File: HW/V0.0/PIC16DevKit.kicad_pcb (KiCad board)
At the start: 4 copper layers, 68.8 x 54 mm, 100 parts, among them J1 9V-12V, J2 USB C, J3 EXP PORT, J4 SIL04, J5 QWIIC, Q1 SI2301, Q3 SI2301, Q4 2N3906, Q5 SI2302, Q6 SI2302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

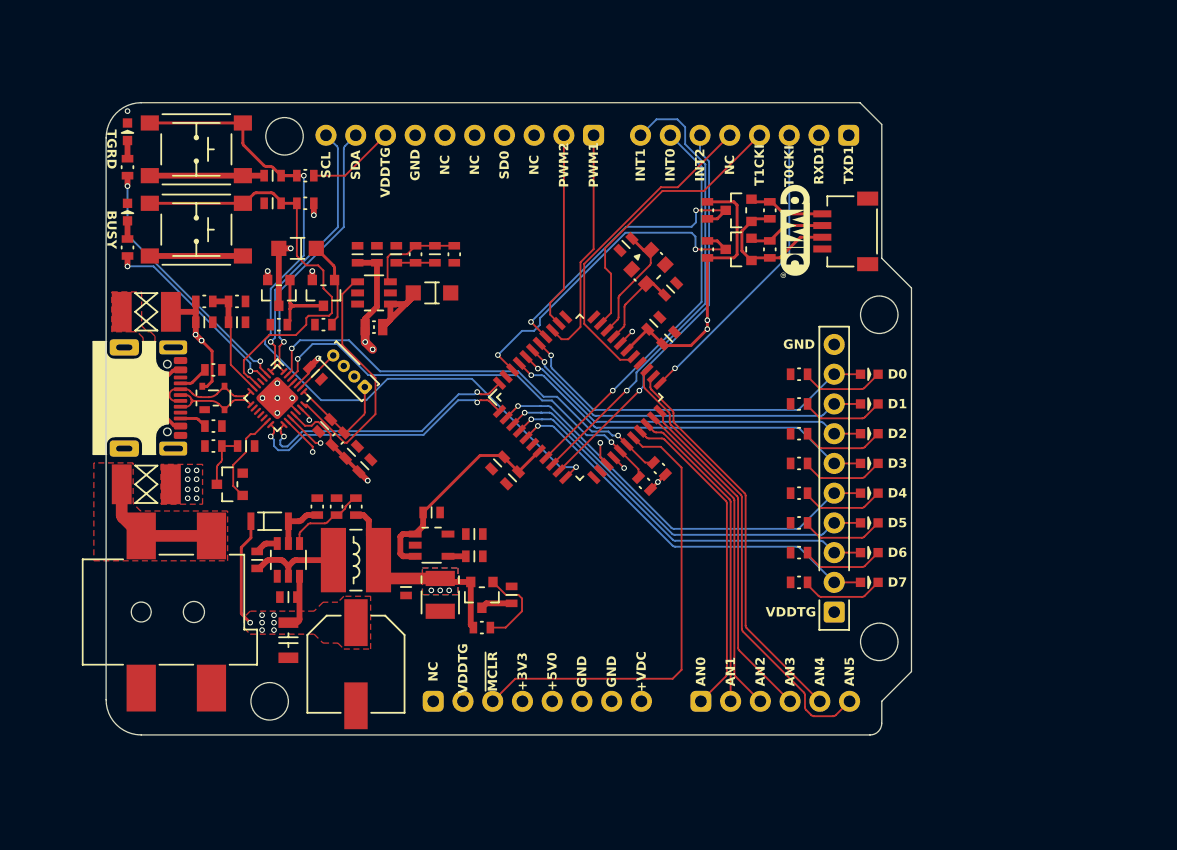
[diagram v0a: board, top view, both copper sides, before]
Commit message: PIC16-DevKit-PCB-877 layout update 2-miss via gnd
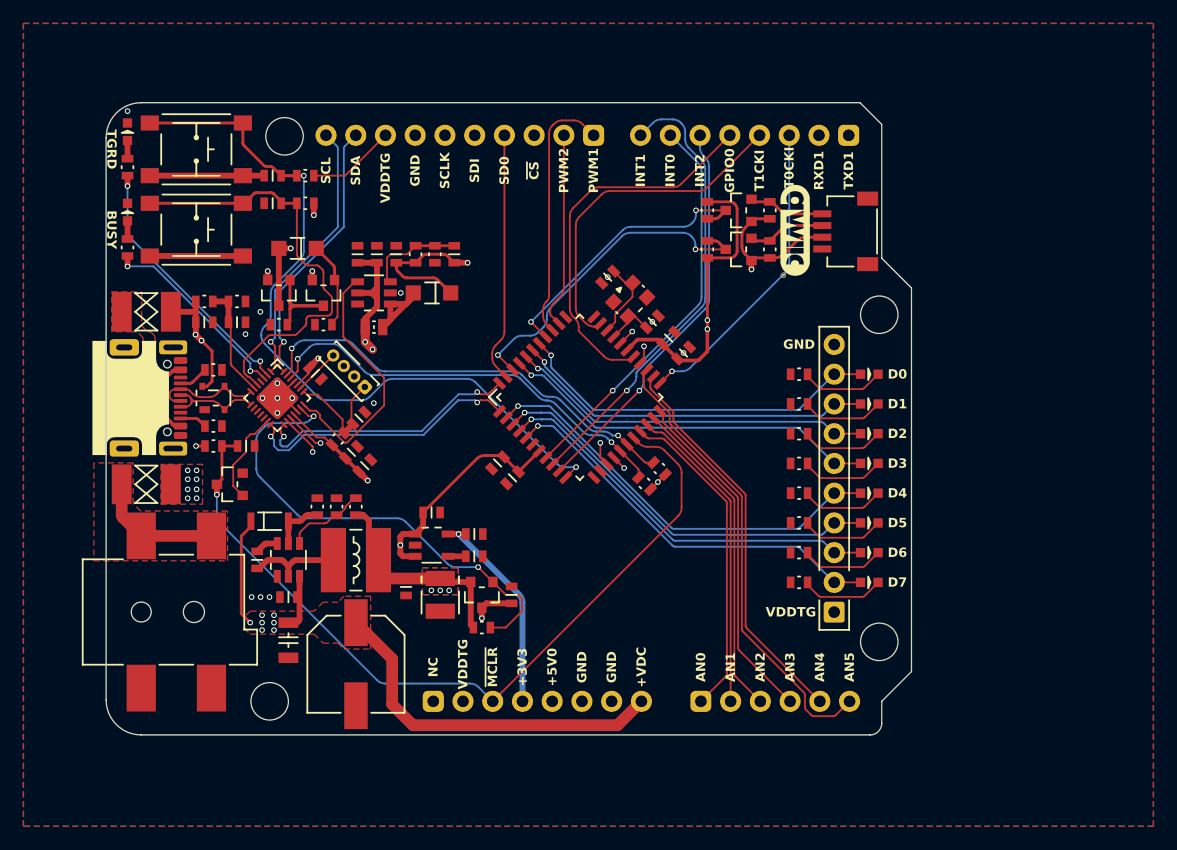
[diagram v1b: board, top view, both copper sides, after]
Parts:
- moved C15 3.20 mm to (107.3, 61.7)
- moved U10 3.20 mm to (105.4, 59.8)
- moved C16 3.20 mm to (103.5, 57.9)
- moved C32 2.99 mm to (82.3, 70.0), turned to -135 degrees
- moved C20 1.80 mm to (108.7, 63.1)
- moved C21 1.80 mm to (110.0, 64.4)
- moved C12 1.65 mm to (90.4, 56.0)
- moved R10 1.65 mm to (88.8, 56.0)
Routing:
- net +3.3V: track 12.5 -> 72.0 mm, vias 0 -> 2
- net VPP: track 3.30 -> 57.8 mm, vias 0 -> 2
- net /TARGET MCU/SCLK: track 1.26 -> 36.5 mm
- net /POWER/~{VTG_EN}: track 8.77 -> 41.4 mm, vias 1 -> 2
- net VDC: track 14.1 -> 45.2 mm
- net /TARGET MCU/SDI: track 2.07 -> 32.7 mm
- net /PROGRAMMER/~{TG_MCLR}: track 44.4 -> 69.3 mm, vias 0 -> 1
- net /TARGET MCU/~{CS}: track 0.00 -> 23.4 mm, vias 0 -> 1
- net +VDDTG: track 198.7 -> 221.2 mm, vias 2 -> 4
- net /TARGET MCU/SDO: track 0.00 -> 21.4 mm
- net /TARGET MCU/T1CKI: track 24.2 -> 29.1 mm
- net /TARGET MCU/GPIO: track 27.7 -> 32.4 mm
- net Net-(U10-GND2): track 7.62 -> 4.21 mm
- net Net-(U10-X1): track 10.4 -> 6.96 mm
- net /TARGET MCU/PWM1: track 20.0 -> 22.1 mm
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- added copper zone on B.Cu, net GND
- added copper zone on F.Cu, net GND
- added copper zone on In1.Cu, net GND
- added copper zone on In2.Cu, net GND
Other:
- board text added: "GPIO0"
- board text added: "SCLK"
- board text added: "SDI"
- board text added: "~{CS}"

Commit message: PIC16-DevKit-PCB-877 layout update 3
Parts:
- turned R1 to -90 degrees
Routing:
- net +VDDTG: track 221.2 -> 182.1 mm, vias 4 -> 6
- net Net-(U2-SW): track 8.06 -> 16.6 mm
- net +5V: track 138.1 -> 144.3 mm
- net GND: track 22.6 -> 28.8 mm, vias 17 -> 16
- net /TARGET MCU/GPIO: track 32.4 -> 28.4 mm
- net +3.3V: track 72.0 -> 76.0 mm, vias 2 -> 3
- net /TARGET MCU/PWM1: track 22.1 -> 19.1 mm
- net /TARGET MCU/T1CKI: track 29.1 -> 26.1 mm
- net /PROGRAMMER/SDA: track 86.4 -> 87.7 mm
- net /PROGRAMMER/SCL: track 77.3 -> 76.0 mm
- net /PROGRAMMER/TXD1: track 68.3 -> 69.0 mm
- net Net-(U2-FB): track 6.94 -> 6.30 mm
- net VDC: track 45.2 -> 44.6 mm, vias 15 -> 11
- added copper zone on B.Cu, net VDC
- added copper zone on In1.Cu, net VDC
